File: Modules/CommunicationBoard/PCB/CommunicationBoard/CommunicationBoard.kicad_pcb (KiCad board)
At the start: 2 copper layers, 50 x 60 mm, 26 parts, among them J1 CIO_MAIN_CONNECTOR, J2 Conn_Coaxial, U1 E22-900M30S

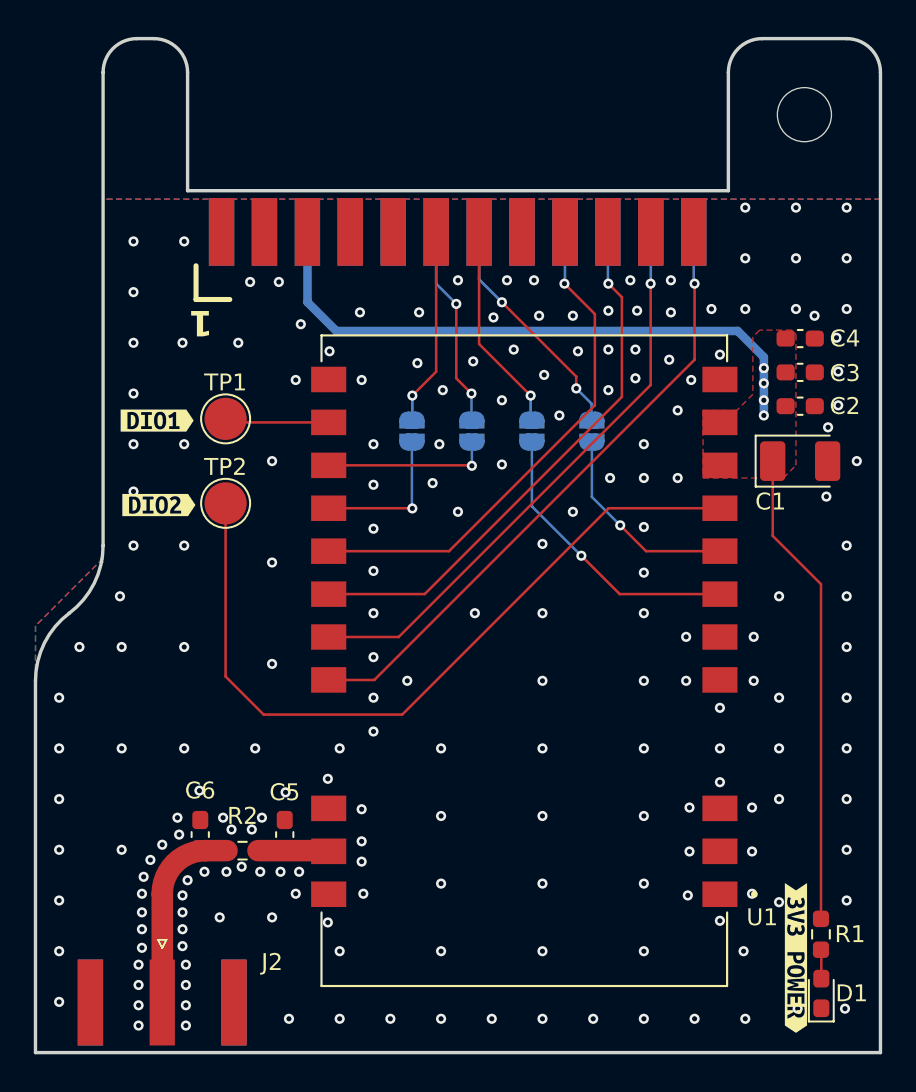
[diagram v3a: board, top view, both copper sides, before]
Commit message: First PCBA with ESP32
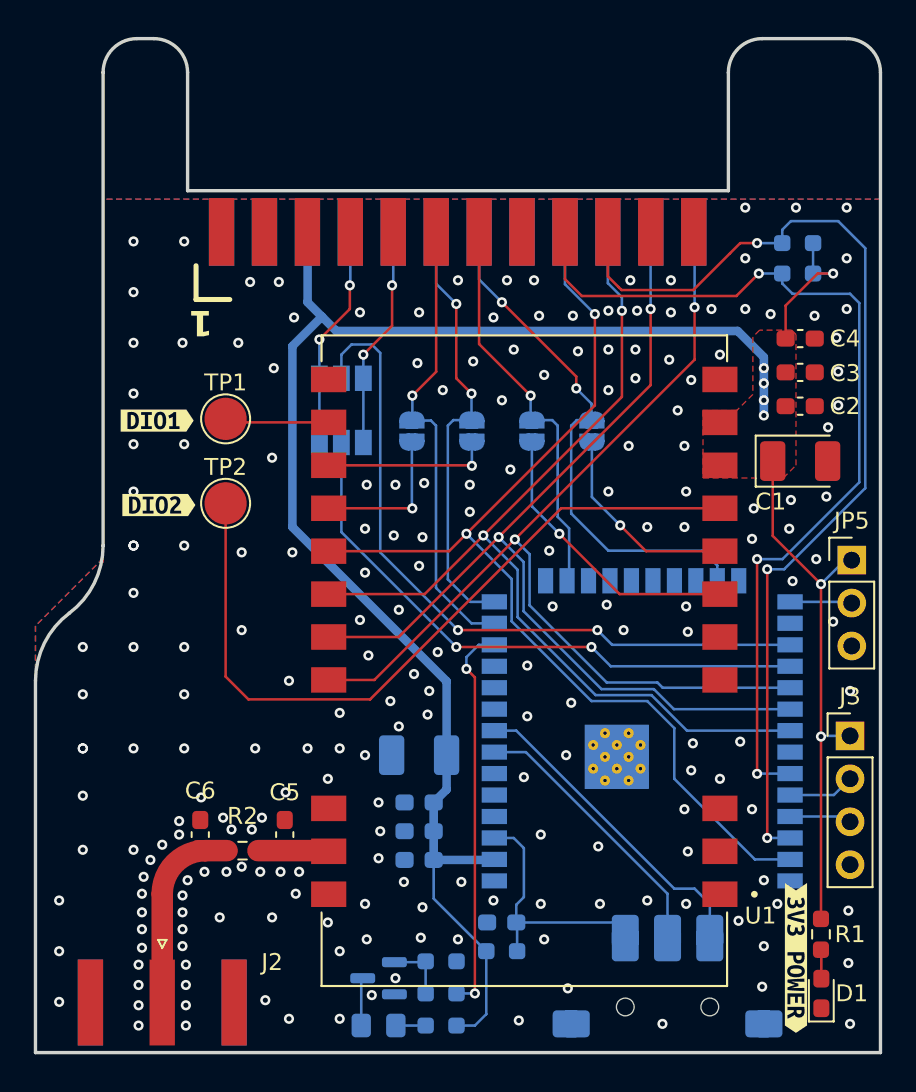
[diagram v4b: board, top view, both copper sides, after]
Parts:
- removed ?: , 
- added C10: 0.1uF, Capacitor_SMD:C_0603_1608Metric_Pad1.08x0.95mm_HandSolder, B.Cu at (147.7, 111.9)
- added C11: 0.1uF, Capacitor_SMD:C_0603_1608Metric_Pad1.08x0.95mm_HandSolder, B.Cu at (147.7, 113.6)
- added C7: 100nF, Capacitor_SMD:C_0603_1608Metric_Pad1.08x0.95mm_HandSolder, B.Cu at (152.6, 117.3)
- added C8: 220u, Capacitor_Tantalum_SMD:CP_EIA-3528-21_Kemet-B_Pad1.50x2.35mm_HandSolder, B.Cu at (147.7, 107.4)
- added C9: 10uF, Capacitor_SMD:C_0603_1608Metric_Pad1.08x0.95mm_HandSolder, B.Cu at (147.7, 110.2)
- added D2: LED, LED_SMD:LED_0805_2012Metric_Pad1.15x1.40mm_HandSolder, B.Cu at (145.3, 123.4)
- added J3: PROGRAMMING, Connector_PinHeader_2.54mm:PinHeader_1x04_P2.54mm_Vertical, F.Cu at (173.2, 106.3)
- added JP5: BOOT_SELECT, Connector_PinHeader_2.54mm:PinHeader_1x03_P2.54mm_Vertical, F.Cu at (173.3, 95.9)
- added JP6: RX, Jumper:SolderJumper-3_P1.3mm_Open_Pad1.0x1.5mm, B.Cu at (143.1, 88.9)
- added JP7: TX, Jumper:SolderJumper-3_P1.3mm_Open_Pad1.0x1.5mm, B.Cu at (143.1, 85.1)
- added Q1: IRLM2502, Package_TO_SOT_SMD:SOT-23, B.Cu at (145.3, 120.6)
- added R3: 10k, Resistor_SMD:R_0603_1608Metric_Pad0.98x0.95mm_HandSolder, B.Cu at (152.6, 119.0)
- added R4: 10k, Resistor_SMD:R_0603_1608Metric_Pad0.98x0.95mm_HandSolder, B.Cu at (170.1, 78.9)
- added R5: 10k, Resistor_SMD:R_0603_1608Metric_Pad0.98x0.95mm_HandSolder, B.Cu at (170.1, 77.1)
- added R6: 2k2, Resistor_SMD:R_0603_1608Metric_Pad0.98x0.95mm_HandSolder, B.Cu at (149.0, 123.4)
- added R7: 220, Resistor_SMD:R_0603_1608Metric_Pad0.98x0.95mm_HandSolder, B.Cu at (149.0, 121.5)
- added R8: 1Meg, Resistor_SMD:R_0603_1608Metric_Pad0.98x0.95mm_HandSolder, B.Cu at (149.0, 119.6)
- added U2: ~, IcaroFootprints:WheelSwitch, B.Cu at (162.4, 122.3)
- added U3: ESP32-WROOM-E, RF_Module:ESP32-WROOM-32UE, B.Cu at (160.9, 106.4)
- moved kibuzzard-67F40C7C 9.30 mm to (147.2, 82.8), turned to -90 degrees
- moved kibuzzard-67F40C92 9.30 mm to (150.7, 82.8), turned to -90 degrees
- moved kibuzzard-67F40CAD 9.30 mm to (154.3, 82.8), turned to -90 degrees
- moved kibuzzard-67F40CB8 9.30 mm to (157.8, 82.8), turned to -90 degrees
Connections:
- J1 pad 10: unconnected-(J1-UART_RX-Pad10) -> /C_UART_RX
- J1 pad 17: unconnected-(J1-SDA_1-Pad17) -> /I2C_EXT.SDA
- J1 pad 19: unconnected-(J1-SCL_1-Pad19) -> /I2C_EXT.SCL
- J1 pad 23: unconnected-(J1-CS1-Pad23) -> /SPI.CS1
- J1 pad 8: unconnected-(J1-UART_TX-Pad8) -> /C_UART_TX
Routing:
- net +3.3V: track 64.2 -> 129.9 mm, vias 4 -> 7
- net /I2C_EXT.SCL: track 0.00 -> 60.2 mm, vias 0 -> 3
- net /I2C_EXT.SDA: track 0.00 -> 55.4 mm, vias 0 -> 3
- net /UART_EXT.RX: track 0.00 -> 42.6 mm, vias 0 -> 2
- net /UART_EXT.TX: track 0.00 -> 35.1 mm, vias 0 -> 2
- net /SPI.MOSI: track 30.3 -> 60.7 mm, vias 1 -> 2
- net /SPI.MISO: track 32.3 -> 56.9 mm, vias 1 -> 2
- net /SPI.SCK: track 34.3 -> 57.5 mm, vias 1 -> 2
- net /LED_PIN: track 0.00 -> 23.1 mm, vias 0 -> 2
- net /SPI.CS0: track 37.1 -> 58.8 mm, vias 1 -> 2
- net Net-(U2-R): track 0.00 -> 19.4 mm
- net /IO3: track 13.9 -> 31.3 mm
- net Net-(U2-Push): track 0.00 -> 16.8 mm
- net /IO0: track 11.7 -> 27.2 mm
- net Net-(U2-L): track 0.00 -> 15.0 mm
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
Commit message: CommsBoard v1.0
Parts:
- J2: footprint Connector_Coaxial:SMA_Amphenol_132289_EdgeMount -> IcaroFootprints:SMA_132323
- moved C5 3.36 mm to (136.4, 112.1)
- moved J2 2.72 mm to (132.5, 124.8), turned to 0 degrees
- moved R2 1.68 mm to (138.9, 113.1)
- moved U3 1.43 mm to (160.9, 105.0)
- moved U2 1.10 mm to (162.4, 121.2)
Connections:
- C5 pad 1: Net-(U1-ANT) -> Net-(J2-In)
- U3 pad 4: unconnected-(U3-SENSOR_VP/GPIO36/ADC1_CH0-Pad4) -> /DIO2
- U3 pad 5: unconnected-(U3-SENSOR_VN/GPIO39/ADC1_CH3-Pad5) -> /DIO1
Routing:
- net /DIO1: track 6.19 -> 45.0 mm, vias 0 -> 1
- net /DIO2: track 44.7 -> 57.4 mm, vias 0 -> 1
- net Net-(U2-L): track 15.0 -> 22.8 mm
- net Net-(U2-R): track 19.4 -> 17.7 mm
- net Net-(J2-In): track 11.5 -> 13.2 mm
- net Net-(U1-ANT): track 4.20 -> 2.57 mm
- net /IO2: track 23.6 -> 22.2 mm
- net /LED_PIN: track 23.1 -> 24.5 mm
- net Net-(U2-Push): track 16.8 -> 15.8 mm
- net /I2C_EXT.SDA: track 55.4 -> 54.6 mm
- net /IO0: track 27.2 -> 26.5 mm
- net /I2C_EXT.SCL: track 60.2 -> 59.5 mm
- net /UART_TX: track 3.68 -> 4.27 mm
- net Net-(JP5-C): track 3.68 -> 4.27 mm
- net /IO3: track 31.3 -> 30.7 mm
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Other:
- board text added: "Comms Board v1.0"
- board text added: "Proyecto Ícaro"

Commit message: Many changes on supply board SW&HW
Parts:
- added REF**: OSHW-Logo2_7.3x6mm_SilkScreen, Symbol:OSHW-Logo2_7.3x6mm_SilkScreen, F.Cu at (129.2, 110.5)
- added REF**: KiCad-Logo2_5mm_SilkScreen, Symbol:KiCad-Logo2_5mm_SilkScreen, F.Cu at (133.4, 103.5)
- added REF**: MountingHole_3.2mm_M3_ISO7380_Pad_TopBottom, MountingHole:MountingHole_3.2mm_M3_ISO7380_Pad_TopBottom, F.Cu at (170.2, 69.6)

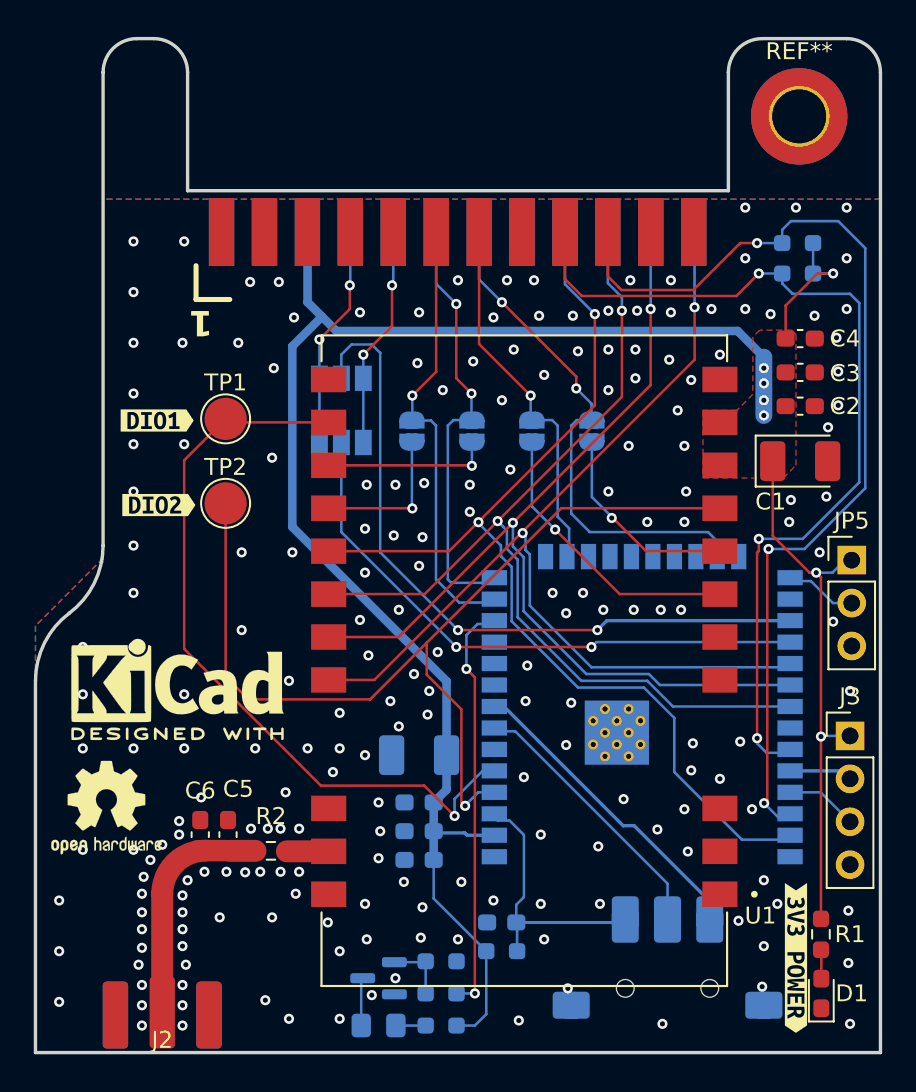
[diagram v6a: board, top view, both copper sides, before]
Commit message: Changed MISO/MOSI in Comms
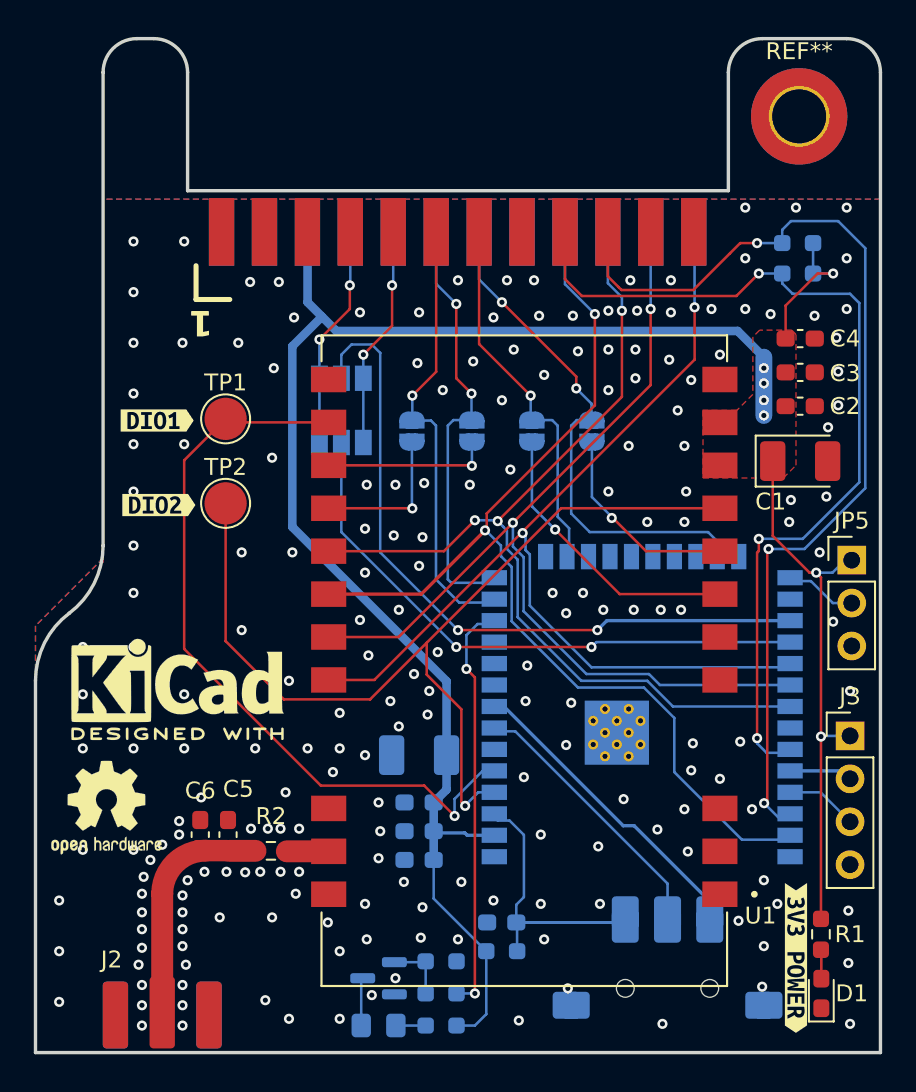
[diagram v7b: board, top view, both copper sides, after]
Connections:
- U1 pad 16: /SPI.MOSI -> /SPI.MISO
- U1 pad 17: /SPI.MISO -> /SPI.MOSI
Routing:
- net /DIO2: track 57.4 -> 56.2 mm
- net /SPI.MISO: track 56.8 -> 55.8 mm, vias 2 -> 3
- net /SPI.MOSI: track 60.9 -> 61.9 mm
- net GND: vias 206 -> 205
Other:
- board text added: "Comms Board v1.1"
- board text removed: "Comms Board v1.0"
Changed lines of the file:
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@@
 		(at 132.5 124.7525)
 		(property "Reference" "J2"
-			(at 0 -0.5 0)
+			(at -3 -5.2525 0)
 			(unlocked yes)
 			(layer "F.SilkS")
@@
 				(font
 					(size 1 1)
-					(thickness 0.1)
+					(thickness 0.15)
 				)
 			)
@@
 			(size 2.08 1.51)
 			(layers "F.Cu" "F.Mask" "F.Paste")
-			(net 4 "/SPI.MOSI")
+			(net 3 "/SPI.MISO")
 			(pinfunction "MISO")
 			(pintype "output")
@@
 			(size 2.08 1.51)
 			(layers "F.Cu" "F.Mask" "F.Paste")
-			(net 3 "/SPI.MISO")
+			(net 4 "/SPI.MOSI")
 			(pinfunction "MOSI")
 			(pintype "input")
@@
 		)
 	)
-	(gr_text "Comms Board v1.0"
+	(gr_text "Comms Board v1.1"
 		(at 149.2 102 0)
 		(layer "B.SilkS")
@@
 	)
 	(via
-		(at 150.7 93)
-		(size 0.6)
-		(drill 0.3)
-		(layers "F.Cu" "B.Cu")
-		(free yes)
-		(net 2)
-	)
-	(via
 		(at 140.2 95.4)
 		(size 0.6)
@@
 	)
 	(segment
-		(start 152.35 93.55)
-		(end 148.03 97.87)
+		(start 149.17 95.33)
+		(end 142.35 95.33)
 		(width 0.1524)
 		(layer "F.Cu")
@@
 	)
 	(segment
-		(start 148.03 97.87)
-		(end 142.35 97.87)
+		(start 151 93.5)
+		(end 149.17 95.33)
 		(width 0.1524)
 		(layer "F.Cu")
@@
 	)
 	(via
+		(at 151 93.5)
+		(size 0.6)
+		(drill 0.3)
+		(layers "F.Cu" "B.Cu")
+		(net 3)
+	)
+	(via
 		(at 159.7 81.1)
 		(size 0.6)
@@
 	)
 	(segment
+		(start 152.3 93.5)
+		(end 152.35 93.55)
+		(width 0.1524)
+		(layer "B.Cu")
+		(net 3)
+	)
+	(segment
 		(start 153.5306 99.2306)
 		(end 153.5306 95.830384)
@@
 	)
 	(segment
+		(start 151 93.5)
+		(end 152.3 93.5)
+		(width 0.1524)
+		(layer "B.Cu")
+		(net 3)
+	)
+	(segment
 		(start 152.8966 94.112885)
 		(end 152.6728 93.889085)
@@
 	)
 	(segment
-		(start 158.1 86.7)
-		(end 158.1 81.3)
+		(start 151.7 93.1)
+		(end 158.1 86.7)
 		(width 0.1524)
 		(layer "F.Cu")
@@
 	)
 	(segment
-		(start 151.212149 93.587851)
-		(end 158.1 86.7)
+		(start 158.1 86.7)
+		(end 158.1 81.3)
 		(width 0.1524)
 		(layer "F.Cu")
@@
 	)
 	(segment
-		(start 151.212149 93.614579)
-		(end 151.212149 93.587851)
-		(width 0.1524)
+		(start 147.83 97.87)
+		(end 142.35 97.87)
+		(width 0.2)
 		(layer "F.Cu")
 		(net 4)
 	)
 	(segment
-		(start 151.212149 93.614579)
-		(end 151.185421 93.614579)
-		(width 0.1524)
+		(start 151.6 94.1)
+		(end 147.83 97.87)
+		(width 0.2)
 		(layer "F.Cu")
 		(net 4)
 	)
 	(segment
-		(start 151.185421 93.614579)
-		(end 149.47 95.33)
+		(start 151.6 94.1)
+		(end 151.7 94)
 		(width 0.1524)
 		(layer "F.Cu")
@@
 	)
 	(segment
-		(start 149.47 95.33)
-		(end 142.35 95.33)
+		(start 151.7 94)
+		(end 151.7 93.1)
 		(width 0.1524)
 		(layer "F.Cu")
@@
 	)
 	(via
-		(at 151.212149 93.614579)
+		(at 151.6 94.1)
 		(size 0.6)
 		(drill 0.3)
@@
 	)
 	(segment
-		(start 152.5432 95)
-		(end 151.212149 93.668949)
+		(start 162.8 108.4)
+		(end 166.8 112.4)
 		(width 0.1524)
 		(layer "B.Cu")
@@
 	)
 	(segment
-		(start 156.33 79.53)
-		(end 156.33 76.4375)
+		(start 153.1772 96.261898)
+		(end 153.1772 99.4772)
 		(width 0.1524)
 		(layer "B.Cu")
@@
 	)
 	(segment
-		(start 162.8 105.2)
-		(end 161 103.4)
+		(start 169.59 112.4)
+		(end 169.65 112.34)
 		(width 0.1524)
 		(layer "B.Cu")
@@
 	)
 	(segment
-		(start 153.1772 99.4772)
+		(start 152.5432 95.627898)
 		(end 153.1772 96.261898)
 		(width 0.1524)
@@
 	)
 	(segment
-		(start 158.1 81.3)
-		(end 156.33 79.53)
+		(start 152.5432 95)
+		(end 152.5432 95.627898)
 		(width 0.1524)
 		(layer "B.Cu")
@@
 	)
 	(segment
-		(start 169.65 112.34)
-		(end 169.59 112.4)
+		(start 157.1 103.4)
+		(end 161 103.4)
 		(width 0.1524)
 		(layer "B.Cu")
@@
 	)
 	(segment
-		(start 169.59 112.4)
-		(end 166.8 112.4)
+		(start 156.33 79.53)
+		(end 156.33 76.4375)
 		(width 0.1524)
 		(layer "B.Cu")
@@
 	)
 	(segment
-		(start 161 103.4)
+		(start 153.1772 99.4772)
 		(end 157.1 103.4)
 		(width 0.1524)
@@
 	)
 	(segment
-		(start 162.8 108.4)
-		(end 162.8 105.2)
+		(start 169.65 112.34)
+		(end 169.65 112.14)
 		(width 0.1524)
 		(layer "B.Cu")
@@
 	)
 	(segment
-		(start 151.212149 93.668949)
-		(end 151.212149 93.614579)
+		(start 162.8 105.2)
+		(end 162.8 108.4)
 		(width 0.1524)
 		(layer "B.Cu")
@@
 	)
 	(segment
-		(start 152.5432 95.627898)
-		(end 152.5432 95)
+		(start 158.1 81.3)
+		(end 156.33 79.53)
 		(width 0.1524)
 		(layer "B.Cu")
@@
 	)
 	(segment
-		(start 153.1772 96.261898)
-		(end 152.5432 95.627898)
+		(start 151.6432 94.1)
+		(end 152.5432 95)
 		(width 0.1524)
 		(layer "B.Cu")
@@
 	)
 	(segment
-		(start 166.8 112.4)
-		(end 162.8 108.4)
+		(start 161 103.4)
+		(end 162.8 105.2)
 		(width 0.1524)
 		(layer "B.Cu")
@@
 	)
 	(segment
-		(start 157.1 103.4)
-		(end 153.1772 99.4772)
+		(start 166.8 112.4)
+		(end 169.59 112.4)
 		(width 0.1524)
 		(layer "B.Cu")
@@
 	)
 	(segment
-		(start 169.65 112.14)
-		(end 169.65 112.34)
+		(start 151.6 94.1)
+		(end 151.6432 94.1)
 		(width 0.1524)
 		(layer "B.Cu")
@@
 	)
 	(segment
-		(start 144.8 104.1)
-		(end 137.6 104.1)
-		(width 0.1524)
-		(layer "F.Cu")
-		(net 26)
-	)
-	(segment
-		(start 137.6 104.1)
-		(end 136.25 102.75)
+		(start 150.2 110.1762)
+		(end 150.2 104.683715)
 		(width 0.1524)
 		(layer "F.Cu")
@@
 	)
 	(segment
-		(start 150.2 110.1762)
-		(end 150.2 104.683715)
+		(start 148.15 102.633715)
+		(end 148.15 100.75)
 		(width 0.1524)
 		(layer "F.Cu")
@@
 	)
 	(segment
-		(start 148.15 102.633715)
-		(end 148.15 100.75)
+		(start 136.25 100.65)
+		(end 136.25 92.5)
 		(width 0.1524)
 		(layer "F.Cu")
@@
 	)
 	(segment
-		(start 148.15 100.75)
-		(end 144.8 104.1)
+		(start 144.8 104.1)
+		(end 139.7 104.1)
 		(width 0.1524)
 		(layer "F.Cu")
@@
 	)
 	(segment
-		(start 136.25 102.75)
-		(end 136.25 92.5)
+		(start 139.7 104.1)
+		(end 136.25 100.65)
+		(width 0.1524)
+		(layer "F.Cu")
+		(net 26)
+	)
+	(segment
+		(start 148.15 100.75)
+		(end 144.8 104.1)
 		(width 0.1524)
 		(layer "F.Cu")
